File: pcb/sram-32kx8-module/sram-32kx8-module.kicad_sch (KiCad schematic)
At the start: 22 parts, among them U1 74LV20, U2 74AHC1G00, U3 62LV256AL45ULI

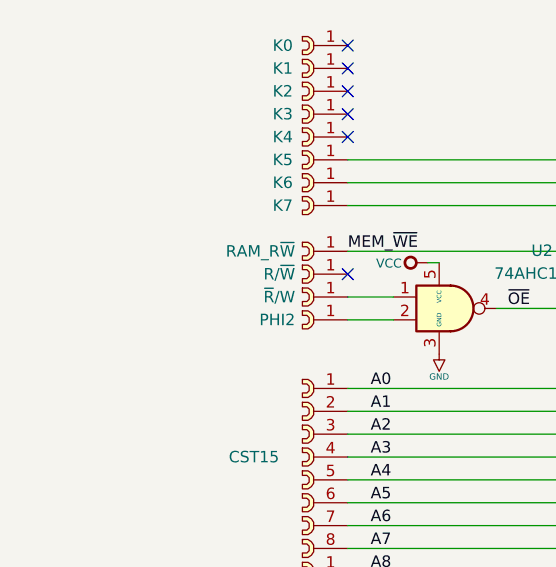
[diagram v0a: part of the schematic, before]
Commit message: Add design note to schematic.
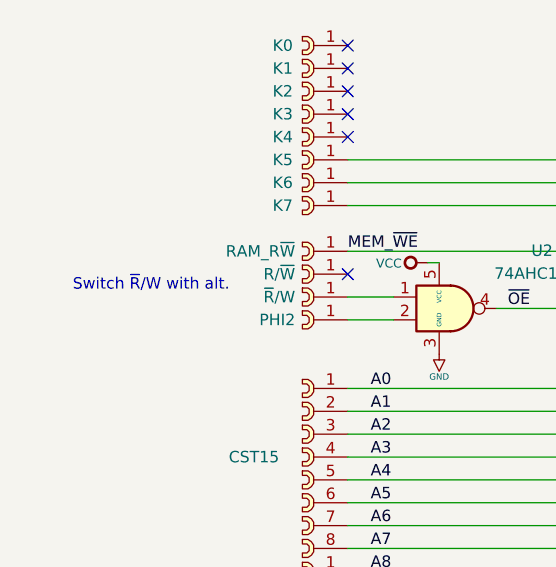
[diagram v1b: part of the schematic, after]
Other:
- note added: "Switch ~{R}/W with alt."
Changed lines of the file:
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@@
 		(company "Circuit Monkey")
+	)
+	(text "Switch ~{R}/W with alt."
+		(exclude_from_sim no)
+		(at 39.116 76.2 0)
+		(effects
+			(font
+				(size 1.27 1.27)
+			)
+		)
 	)
 	(text "SRAM is all of lower 32K address space,\nexcept 0x1400 to 0x1FFF ( K5, K6, K7 ) \nfor KIM-1 ROM and I/O."

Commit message: Add rework note.
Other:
- note added: "Change OE to R/W direct. - Remove U2 - Bridge U2.1 to U2.4"
- note removed: "Switch ~{R}/W with alt."
- title: SRAM Module, 32Kx8, for KIM-1 -> SRAM Module, 32Kx8, for KIM-1000
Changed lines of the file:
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@@
 	(paper "A4")
 	(title_block
-		(title "SRAM Module, 32Kx8, for KIM-1")
-		(rev "A")
+		(title "SRAM Module, 32Kx8, for KIM-1000")
+		(date "2025-09-03")
+		(rev "B")
 		(company "Circuit Monkey")
 	)
-	(text "Switch ~{R}/W with alt."
+	(text "Change OE to R/W direct.\n- Remove U2\n- Bridge U2.1 to U2.4\n"
 		(exclude_from_sim no)
 		(at 39.116 76.2 0)
